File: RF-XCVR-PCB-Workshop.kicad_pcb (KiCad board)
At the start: 4 copper layers, 93.9 x 97.3 mm, 68 parts, among them J1 Screw_Terminal_01x02, J2 Screw_Terminal_01x02, J3 Conn_Coaxial, J4 Conn_01x12_Pin, U1 CC1101RGP, U2 SKY65366-21, U3 PE4251MLI-Z, U4 NCP186AMX390TAG, Y1 NX3225GA-26MHZ-TI

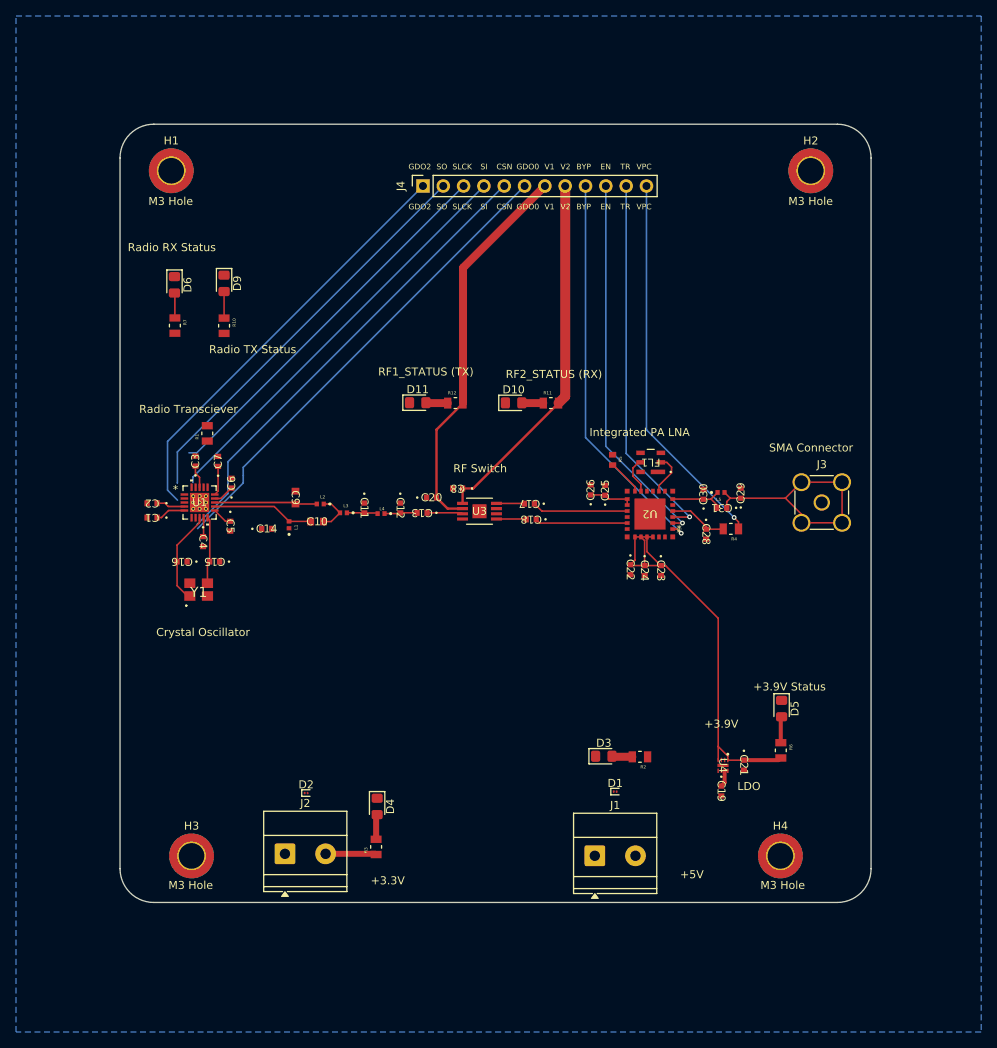
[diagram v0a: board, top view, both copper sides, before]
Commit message: bare CC1101 XCVR laid out
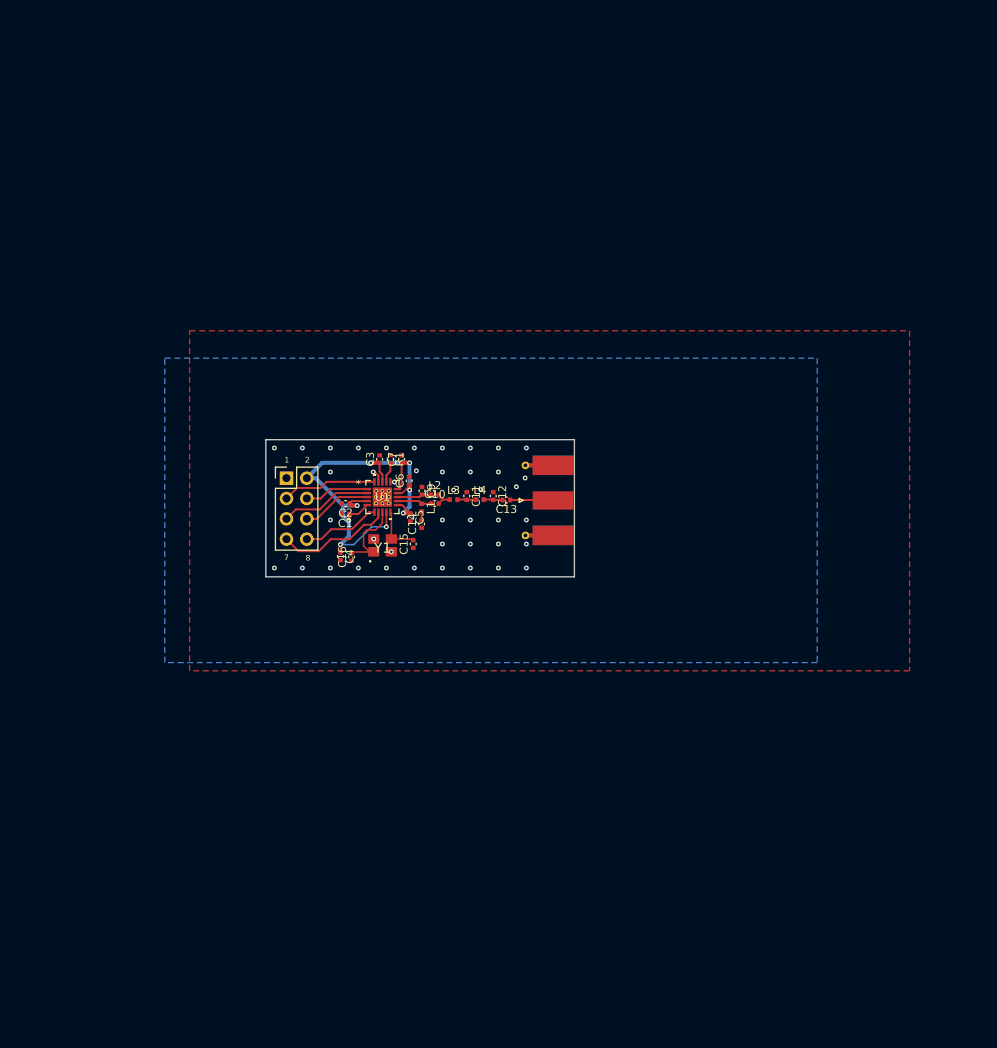
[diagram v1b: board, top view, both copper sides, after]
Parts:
- removed C17, C18: 68pF, comms-board-footprints-passives:G-188_MUR-L-100nF-GRM188
- removed C19, C21, C24: 1uF, comms-board-footprints-passives:G-188_MUR-L-100nF-GRM188
- removed C20, C22, C25, C8: 220pF, comms-board-footprints-passives:G-188_MUR-L-100nF-GRM188
- removed C23: 1nF, comms-board-footprints-passives:G-188_MUR-L-100nF-GRM188
- removed C26: 10nF, comms-board-footprints-passives:G-188_MUR-L-100nF-GRM188
- removed C28: 4.7nF, comms-board-footprints-passives:G-188_MUR-L-100nF-GRM188
- removed C29, C30: 6.8pF, comms-board-footprints-passives:G-188_MUR-L-100nF-GRM188
- removed C31: 3pF, comms-board-footprints-passives:G-188_MUR-L-100nF-GRM188
- removed D1, D2: ESD131-B1-W0201, Diode_SMD:Infineon_SG-WLL-2-3_0.58x0.28_P0.36mm
- removed D10, D11, D3, D4, D5, D6, D9: LED, LED_SMD:LED_0805_2012Metric_Pad1.15x1.40mm_HandSolder
- removed FL1: B39431R0900U410_6-SMD, comms-board-footprints:B39431R0900U410_QUA
- removed H1, H2, H3, H4: MountingHole, MountingHole:MountingHole_3.2mm_M3_DIN965_Pad_TopBottom
- removed J2: Screw_Terminal_01x02, TerminalBlock_Phoenix:TerminalBlock_Phoenix_MKDS-1,5-2-5.08_1x02_P5.08mm_Horizontal
- removed J4: Conn_01x12_Pin, Connector_PinSocket_2.54mm:PinSocket_1x12_P2.54mm_Vertical
- removed L5: 12nH, comms-board-footprints-passives:INDC1005X55N
- removed R10, R11, R12, R2, R3, R4, R6, R7: 220, comms-board-footprints-passives:RESC2012X60N
- removed R5: 0, comms-board-footprints:CAPC1005X60
- removed U2: SKY65366-21, comms-board-footprints:SKY65366-21_SKY
- removed U3: PE4251MLI-Z, comms-board-footprints:8-MSOP_PE4251_PSM
- removed U4: NCP186AMX390TAG, comms-board-footprints:XDFN8_1P7X1P3_ONS
- C1, C11, C12, C13, C14, C15, C16, C2, C3, C4, C5, C6, C7: footprint comms-board-footprints-passives:G-188_MUR-L-100nF-GRM188 -> Capacitor_SMD:C_0402_1005Metric
- C10, C9: footprint comms-board-footprints-passives:CAP_600S0R1AT250XT_ATC -> Capacitor_SMD:C_0402_1005Metric
- J1: value Screw_Terminal_01x02 -> Conn_02x04_Odd_Even; footprint TerminalBlock_Phoenix:TerminalBlock_Phoenix_MKDS-1,5-2-5.08_1x02_P5.08mm_Horizontal -> Connector_PinHeader_2.54mm:PinHeader_2x04_P2.54mm_Vertical
- J3: footprint Connector_Coaxial:SMA_Amphenol_132134-11_Vertical -> Connector_Coaxial:SMA_Molex_73251-1153_EdgeMount_Horizontal
- L1, L2, L3, L4: footprint comms-board-footprints-passives:INDC1005X55N -> Inductor_SMD:L_0402_1005Metric
- R1: footprint comms-board-footprints-passives:RESC2012X60N -> Resistor_SMD:R_0402_1005Metric
- moved J1 60.9 mm to (78.3, 89.5)
- moved J3 35.3 mm to (109.8, 92.3), turned to 180 degrees
- moved C15 24.9 mm to (94.1, 97.8), turned to 90 degrees
- moved C2 24.2 mm to (85.7, 92.7)
- moved C1 24.1 mm to (85.6, 94.0)
- moved Y1 23.6 mm to (90.3, 97.9)
- moved R1 23.1 mm to (91.2, 87.2), turned to -90 degrees
- moved C3 23.0 mm to (89.9, 87.2)
- moved C7 22.9 mm to (92.7, 87.2)
- moved U1 22.9 mm to (90.2, 91.9)
- moved C5 22.5 mm to (93.8, 94.4)
- moved C6 22.2 mm to (93.6, 89.8)
- moved C16 21.2 mm to (86.4, 99.4), turned to 90 degrees
- moved C14 19.4 mm to (95.2, 95.2), turned to 90 degrees
- moved C4 17.3 mm to (85.0, 99.3)
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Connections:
- J1 pad 2: +5V -> +3.3V
- J3 pad 1: GND -> RFC
- J3 pad 2: Net-(J3-Ext) -> GND
- R1 pad 1: Net-(U1-RBIAS) -> GND
- R1 pad 2: GND -> Net-(U1-RBIAS)
- U1 pad 2: SO -> MISO
- U1 pad 20: SI -> MOSI
- U1 pad V: (no net) -> GND
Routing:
- net +3.9V: track 54.4 -> 0.00 mm
- net SI: track 52.1 -> 0.00 mm
- net SO: track 50.9 -> 0.00 mm
- net GD00: track 59.8 -> 9.84 mm
- net TR: track 49.6 -> 0.00 mm, vias 1 -> 0
- net V1: track 48.4 -> 0.00 mm
- net VPC: track 47.6 -> 0.00 mm, vias 1 -> 0
- net EN: track 47.3 -> 0.00 mm, vias 1 -> 0
- net BYP: track 46.8 -> 0.00 mm, vias 1 -> 0
- net V2: track 45.8 -> 0.00 mm
- net GD02: track 53.0 -> 8.68 mm
- net CSN: track 58.3 -> 14.5 mm
- net SCLK: track 48.2 -> 8.04 mm
- net Net-(J3-Ext): track 31.3 -> 0.00 mm
- net +3.3V: track 33.3 -> 64.0 mm, vias 0 -> 8
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- added copper zone on F.Cu, net GND
- removed copper zone on In2.Cu, net +3.3V
- removed copper zone on In1.Cu, net GND
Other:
- board size 93.9 x 97.3 mm -> 38.6 x 17.1 mm
- copper layers 4 -> 2
- board text added: "1"
- board text added: "2"
- board text added: "7"
- board text added: "8"
- board text removed: "+3.3V"
- board text removed: "+3.9V"
- board text removed: "+3.9V Status"
- board text removed: "+5V"
- board text removed: "BYP"
- board text removed: "Board edges fillet = 4.219 mm"
- board text removed: "CSN"
- board text removed: "Crystal Oscillator"
- board text removed: "EN"
- board text removed: "GDO0"
- board text removed: "GDO2"
- board text removed: "Integrated PA LNA"
- board text removed: "LDO"
- board text removed: "M3 Hole"
- board text removed: "RF Switch"
- board text removed: "RF1_STATUS (TX)"
- board text removed: "RF2_STATUS (RX)"
- board text removed: "Radio RX Status"
- board text removed: "Radio TX Status"
- board text removed: "Radio Transciever"
- board text removed: "SI"
- board text removed: "SLCK"
- board text removed: "SMA Connector"
- board text removed: "SO"
- board text removed: "TR"
- board text removed: "V1"
- board text removed: "V2"
- board text removed: "VPC"
